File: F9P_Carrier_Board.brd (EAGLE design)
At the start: 56.8 x 66 mm, 92 parts, among them J4 U.FL, J5 QWIIC_RIGHT_ANGLE, J6 MICROMOD-2222-C, J8 JTAG, U1 U-BLOX_ZED-F9P, U5 AP7361C-33

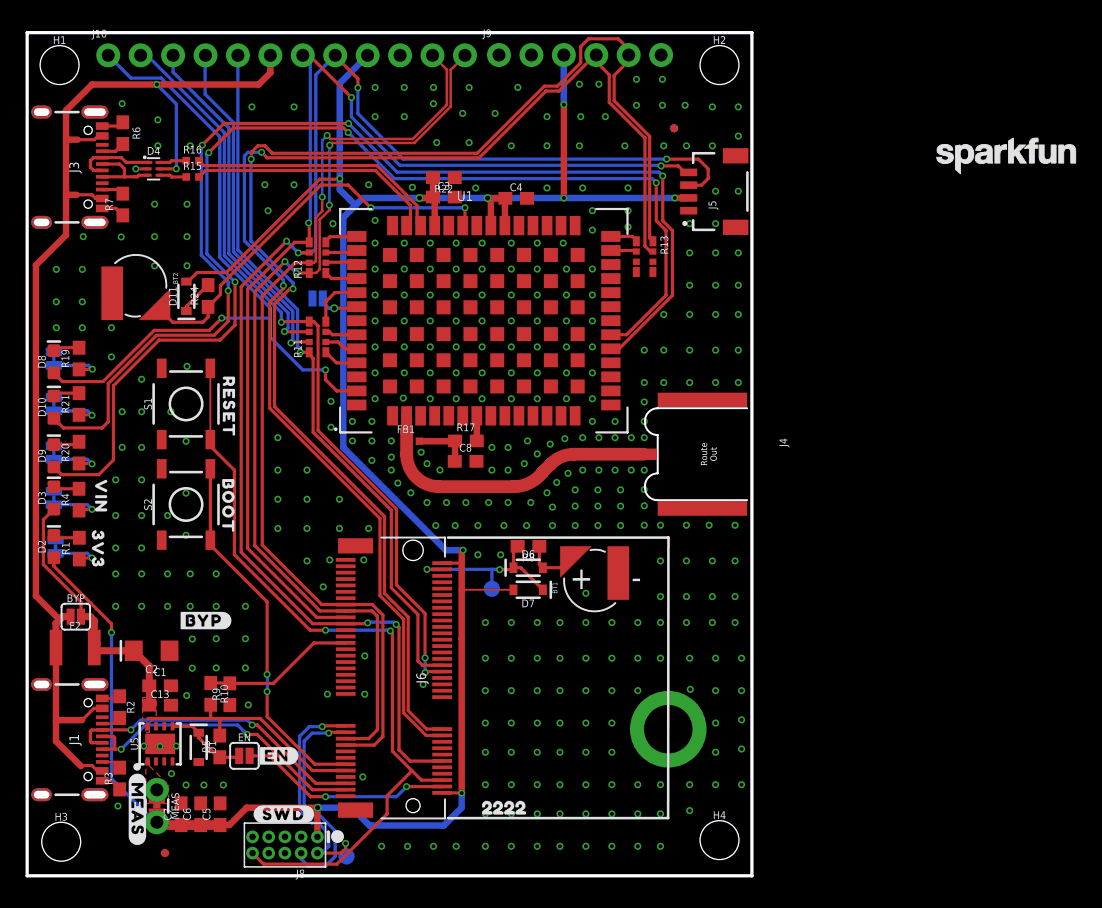
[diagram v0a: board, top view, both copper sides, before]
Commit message: Adds even more vias
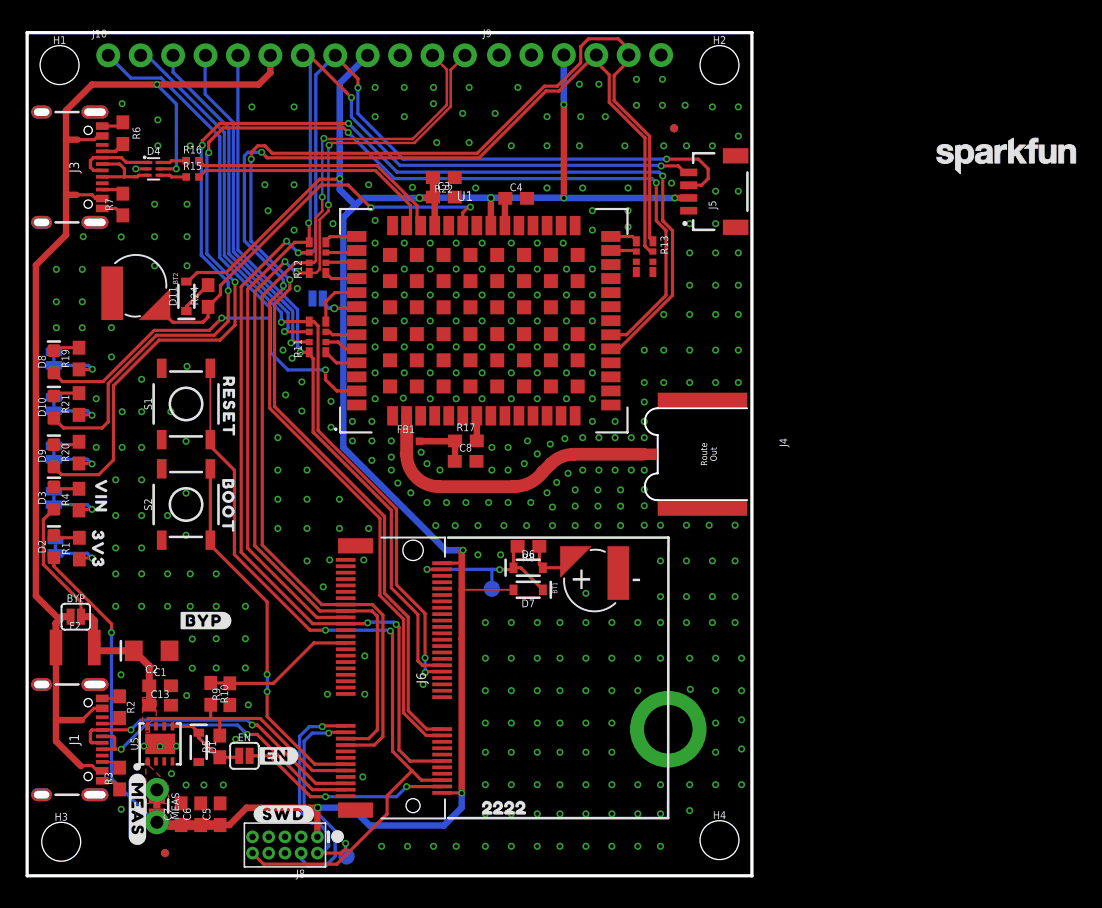
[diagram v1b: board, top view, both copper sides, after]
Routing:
- net 3.3V: track 190.7 -> 189.2 mm
- net V_BATT: track 32.0 -> 32.7 mm
- net PPS: track 57.0 -> 57.7 mm
- net GND: vias 380 -> 392

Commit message: Adds silk and measures
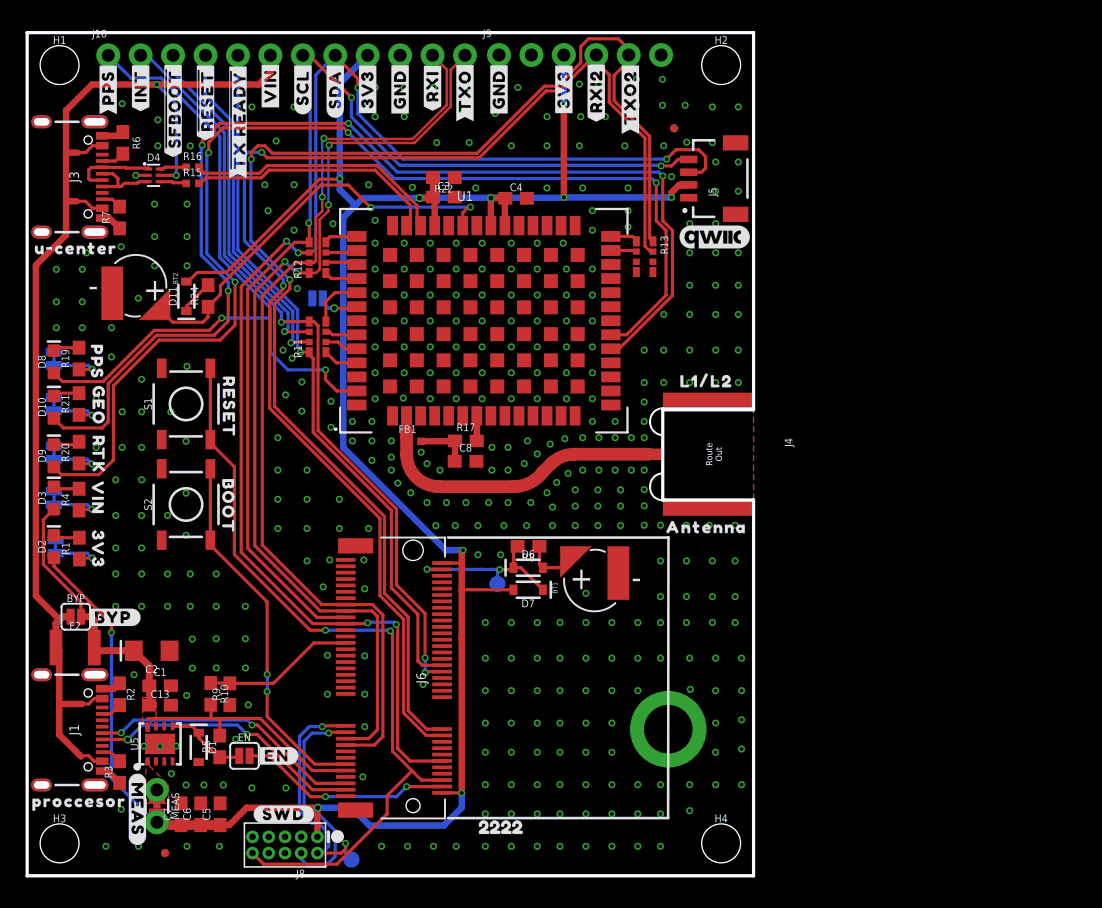
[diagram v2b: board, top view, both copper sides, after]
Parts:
- added U$1: (no value), top:##RESET##11
- added U$10: (no value), top:#RXI#8
- added U$11: (no value), top:#RXI2#9
- added U$12: (no value), top:#SCL#5
- added U$13: (no value), top:#SDA#4
- added U$14: (no value), top:#TXO#7
- added U$15: (no value), top:#TXO2#9
- added U$16: (no value), bot:#SDO#5
- added U$17, U$35: (no value), top:#VIN#13
- added U$18: (no value), top:GEO15
- added U$19: (no value), top:PPS14
- added U$2: (no value), top:##SFBOOT##10
- added U$20: (no value), top:RTK16
- added U$21: (no value), bot:#SDI#6
- added U$22: (no value), bot:#CLK#2
- added U$23: (no value), bot:#GEO#9
- added U$24: (no value), bot:##TX_READY##7
- added U$25: (no value), bot:##SFBOOT##8
- added U$26: (no value), bot:#PPS#10
- added U$27: (no value), bot:#RTK#8
- added U$28: (no value), bot:##CS##2
- added U$29: (no value), bot:#INT#4
- added U$3, U$31, U$32, U$4: (no value), top:#3V3#1
- added U$30: (no value), bot:#SPI#11
- added U$33, U$34, U$6, U$7: (no value), top:#GND#0
- added U$36: (no value), top:#INT#10
- added U$37: (no value), bot:#PPS#3
- added U$38: (no value), bot:#TXO2#10
- added U$40: (no value), bot:#RXI2#10
- added U$41: (no value), bot:##RESET##9
- added U$44: (no value), top:ZED#F9P19
- added U$45: (no value), top:GPS19
- added U$46: (no value), top:L1#L215
- added U$47: (no value), top:ANTENNA15
- added U$49: (no value), top:U#CENTER20
- added U$50: (no value), SparkFun-Aesthetics:QWIIC_5.5MM
- added U$52: (no value), top:PROCCESOR21
- added U$8: (no value), top:##TX_READY##13
- added U$9: (no value), top:#PPS#6
- LOGO1: value SFE_LOGO_NAME.1_INCH -> SFE_LOGO_NAME_FLAME.3_INCH; device SparkFun-Aesthetics:SFE_LOGO_NAME_.1 -> SparkFun-Aesthetics:SFE_LOGO_NAME_FLAME_.3
- moved LOGO1 51.5 mm to (31.1, 32.5), flipped to the bottom
- moved FRAME1 17.9 mm to (3.05, -19.3)
- moved U$39 7.12 mm to (6.73, 20.2)
- moved U$55 1.55 mm to (34.4, 3.81)
- moved R7 1.05 mm to (7.24, 51.6)
- moved R2 1.02 mm to (7.24, 14.2)
- moved J5 1.02 mm to (51.8, 54.6)
- moved J1 0.76 mm to (6.22, 11.4)
- moved J3 0.76 mm to (6.22, 54.7)
- moved R6 0.76 mm to (7.49, 57.4)
- moved TP1 0.58 mm to (36.8, 22.9)
- moved D4 0.51 mm to (9.91, 54.9)
- moved R15 0.51 mm to (13.0, 54.2)
- moved R3 0.51 mm to (7.24, 8.13)
- moved R16 0.51 mm to (13.0, 55.5)
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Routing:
- net USB_N: track 24.2 -> 21.5 mm
- net USB_P: track 23.9 -> 21.6 mm
- net 3.3V: track 189.2 -> 189.9 mm
- net N$24: track 3.32 -> 2.68 mm
- net V_USB: track 94.0 -> 93.4 mm
- net RTC_3V: track 14.5 -> 14.0 mm
- net GND: track 7.59 -> 7.23 mm, vias 392 -> 404
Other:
- board size 56.8 x 66 mm -> 56.9 x 66 mm

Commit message: Fixes nets on the ZED-F9P, fixes silk, removes excessive GND vias, adds SMA connector for PPS
* Fixes 12 pin header
* Fixes jumper labels in schematic
* Fixes RX/TX lines, and SDO/SDI lines
* Adds version number
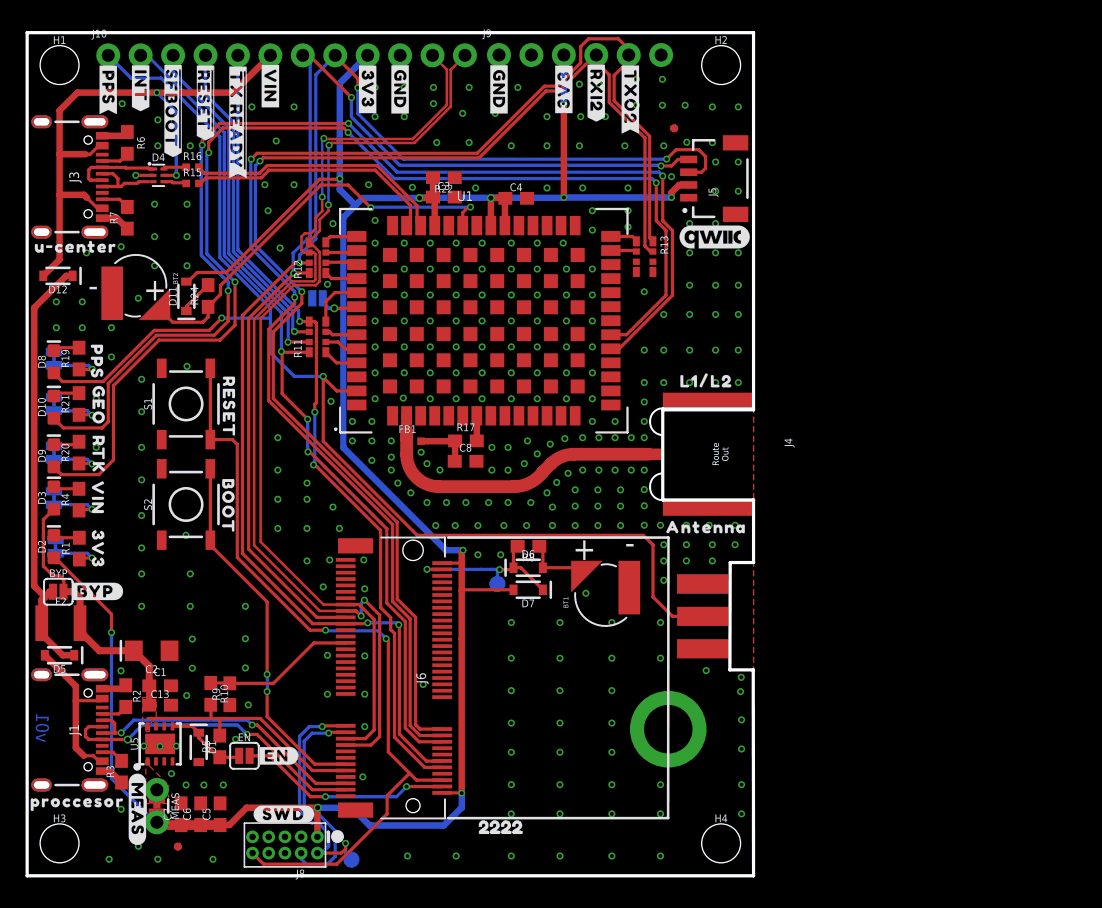
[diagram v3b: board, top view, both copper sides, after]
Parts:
- removed U$10: (no value), top:#RXI#8
- removed U$12: (no value), top:#SCL#5
- removed U$13: (no value), top:#SDA#4
- removed U$14: (no value), top:#TXO#7
- removed U$16: (no value), bot:#SDO#5
- removed U$21: (no value), bot:#SDI#6
- removed U$22: (no value), bot:#CLK#2
- removed U$28: (no value), bot:##CS##2
- added D12, D5: 3A/10V/280mV, SparkFun-DiscreteSemi:SOD-323
- added E1: ANTENNA-SMA-GROUNDEDEDGE_SMA, SparkFun-RF:SMA-EDGE
- J10: device SparkFun-Connectors:1X12_NO_SILK_KIT -> SparkFun-Connectors:1X12_NO_SILK
- moved U$39 2.45 mm to (5.36, 22.3)
- moved BYP 2.39 mm to (2.44, 22.3)
- moved F2 2.21 mm to (2.64, 19.8)
- moved LOGO3 2.11 mm to (2.16, 22.1)
- moved U$44 1.52 mm to (21.2, 28.2)
- moved BT1 1.43 mm to (45.3, 22.0)
- moved FD1 1.14 mm to (11.8, 2.29)
- moved FD3 1.14 mm to (11.8, 2.29)
- moved R7 0.61 mm to (7.85, 51.5)
- moved R2 0.51 mm to (7.72, 14.1)
- moved D4 0.38 mm to (10.3, 54.9)
- moved R6 0.36 mm to (7.85, 57.4)
- moved R3 0.15 mm to (7.39, 8.15)
- moved U$49 0.13 mm to (3.81, 49.3)
- moved U$52 0.13 mm to (3.94, 5.84)
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- renumbered JP5 to SPI
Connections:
- new net V_FUSE: BYP.1, D12.C, D5.C, F2.1
- new net V_USB_2: D12.A, D4.5, J10.6, J3.VBUS1, J3.VBUS2
- net !SAFEBOOT!: now also R11.P7; no longer R11.P6
- net !ZED_RESET!: now also R11.P6; no longer R11.P7
- net GND: now also E1.GND@0, E1.GND@1, E1.GND@2, E1.GND@3
- net INT: now also J6.18, R11.P8; no longer J6.40, R11.P5
- net PPS: now also E1.SIG
- net RXI/SDI: now also J6.59, R12.P6; no longer J6.61, R12.P7
- net RXI2: now also J6.22; no longer J6.20
- net SCL/CLK: now also R12.P8; no longer R12.P5
- net SDA/!CS!: now also R12.P7; no longer R12.P6
- net TXO/SDO: now also J6.61, R12.P5; no longer J6.59, R12.P8
- net TXO2: now also J6.20; no longer J6.22
- net TX_READY: now also J6.10, R11.P5; no longer J6.42, R11.P8
- net V_USB: now also D5.A; no longer BYP.1, D4.5, F2.1, J10.6, J3.VBUS1, J3.VBUS2
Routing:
- net V_USB: track 93.4 -> 12.9 mm, vias 2 -> 0
- net V_USB_2: track 0.00 -> 47.4 mm, vias 0 -> 2
- net PPS: track 57.7 -> 99.8 mm
- net V_FUSE: track 0.00 -> 33.6 mm
- net TX_READY: track 55.7 -> 64.2 mm, vias 1 -> 3
- net INT: track 60.8 -> 67.1 mm
- net RXI/SDI: track 74.2 -> 78.0 mm, vias 2 -> 4
- net USB_P: track 21.6 -> 25.0 mm
- net SDA/!CS!: track 110.4 -> 107.3 mm, vias 6 -> 5
- net TXO/SDO: track 75.3 -> 72.8 mm, vias 4 -> 2
- net USB_N: track 21.5 -> 23.4 mm
- net GND: track 7.23 -> 9.00 mm, vias 404 -> 335
- net RXI2: track 102.1 -> 100.8 mm
- net !ZED_RESET!: track 26.9 -> 25.8 mm
- net TXO2: track 104.7 -> 105.4 mm
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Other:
- outline, holes or cut-outs redrawn
- board text added: "v01"

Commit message: Fixes silk, updates schematic with better labels and descriptions
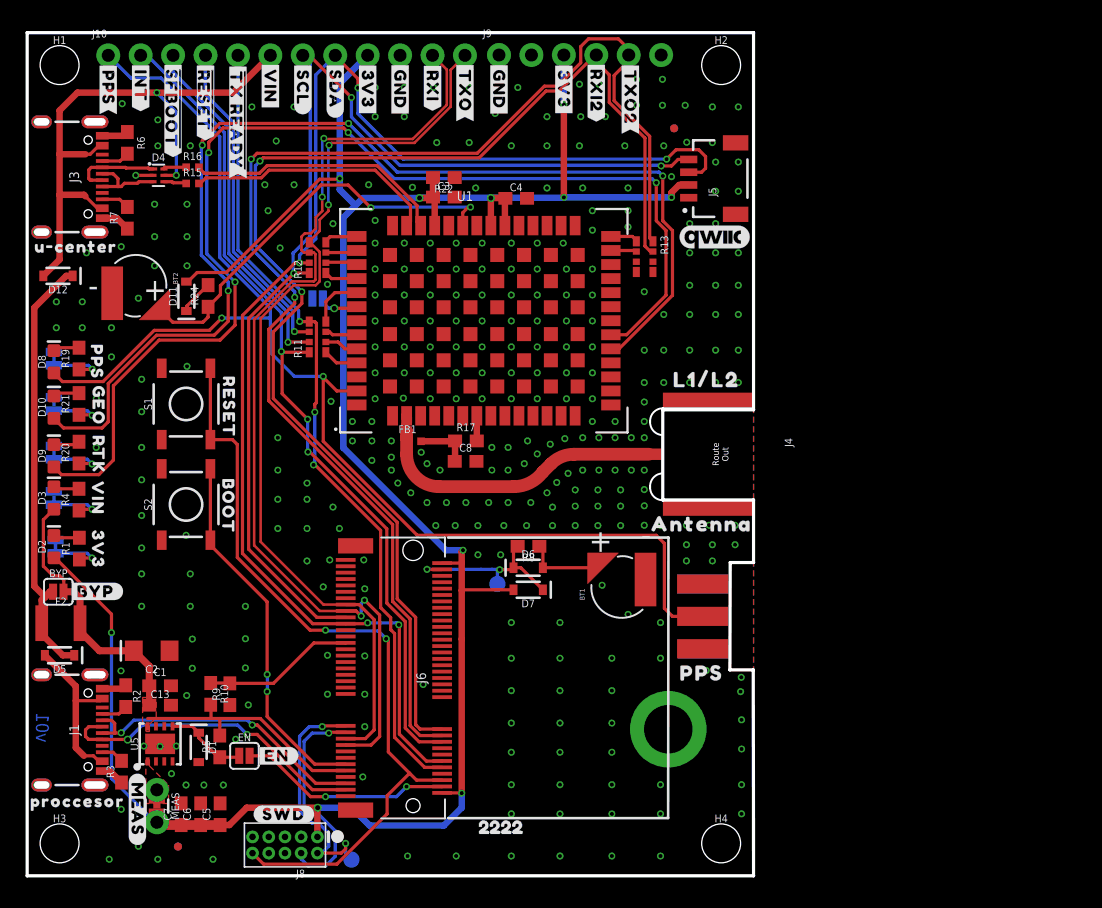
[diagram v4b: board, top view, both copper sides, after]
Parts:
- added U$10: (no value), bot:#SCL#1
- added U$12: (no value), bot:#SDA#0
- added U$13: (no value), bot:#TXO#5
- added U$14: (no value), bot:#RXI#6
- added U$16: (no value), top:PPS15
- added U$21: (no value), top:ANTENNA16
- added U$22: (no value), top:L1#L216
- added U$28: (no value), top:##CS##9
- added U$53: (no value), top:#SDI#11
- added U$54: (no value), top:BLUETOOTH24
- added U$56: (no value), top:U#CENTER22
- added U$57: (no value), top:PROCCESOR23
- added U$58: (no value), top:L1#L217
- added U$59: (no value), top:ANTENNA17
- added U$60: (no value), top:PPS16
- U$46: device top:L1#L215 -> top:#CLK#7
- U$47: device top:ANTENNA15 -> top:#SDO#9
- moved U$47 39.2 mm to (34.3, 61.6), flipped to the bottom, turned to 90 degrees
- moved U$46 39.1 mm to (21.6, 61.7), flipped to the bottom, turned to 90 degrees
- moved BT1 1.42 mm to (46.6, 22.6)
- turned U$132 to 90 degrees
- turned U$3 to 90 degrees
- turned U$32 to 270 degrees
- turned U$4 to 90 degrees
- turned U$6 to 90 degrees
- turned U$7 to 90 degrees
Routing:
- net N$14: track 4.74 -> 6.16 mm
- net PPS: track 99.8 -> 100.7 mm
- net 3.3V: track 190.0 -> 189.4 mm
- net GND: track 9.00 -> 9.57 mm, vias 335 -> 332
- net V_FUSE: track 33.6 -> 34.1 mm
